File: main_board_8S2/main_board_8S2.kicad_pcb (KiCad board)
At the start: 2 copper layers, 114.3 x 86.4 mm, 47 parts

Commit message: Схемы и платы обновлены в связи с переименованием футпринта стойки VMH-STA-DA5
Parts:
- VMH1, VMH2, VMH3, VMH4: footprint KCL:STA-DA5 -> KCL:VMH-STA-DA5

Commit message: Платы скорректированы с учётом изменений в ФП переключателей
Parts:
- SA1, SA2: value SWITCH_SPECIAL_SK-42D01-G -> SWITCH_GENERAL_04P_02T
- SA3: value SWITCH_BLOCK_05 -> SWITCH_GENERAL_01P_01T_NO_05U
- SB1: value SWITCH_BUTTON_NO_01 -> SWITCH_BUTTON_NON-LOCK_01P_01T_NO
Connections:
- XP2 pad 1: Net-(SA2-Pad11) -> Net-(SA2-PadCOM2)
- XP2 pad 2: Net-(SA2-Pad2) -> Net-(SA2-PadCOM1)
- XS2 pad 1: Net-(SA2-Pad11) -> Net-(SA2-PadCOM2)
- XS2 pad 2: Net-(SA2-Pad2) -> Net-(SA2-PadCOM1)
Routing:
- net Net-(SA2-PadCOM1): track 0.00 -> 96.5 mm
- net Net-(SA2-Pad2): track 96.5 -> 0.00 mm
- net Net-(SA2-PadCOM2): track 0.00 -> 56.0 mm
- net Net-(SA2-Pad11): track 56.0 -> 0.00 mm

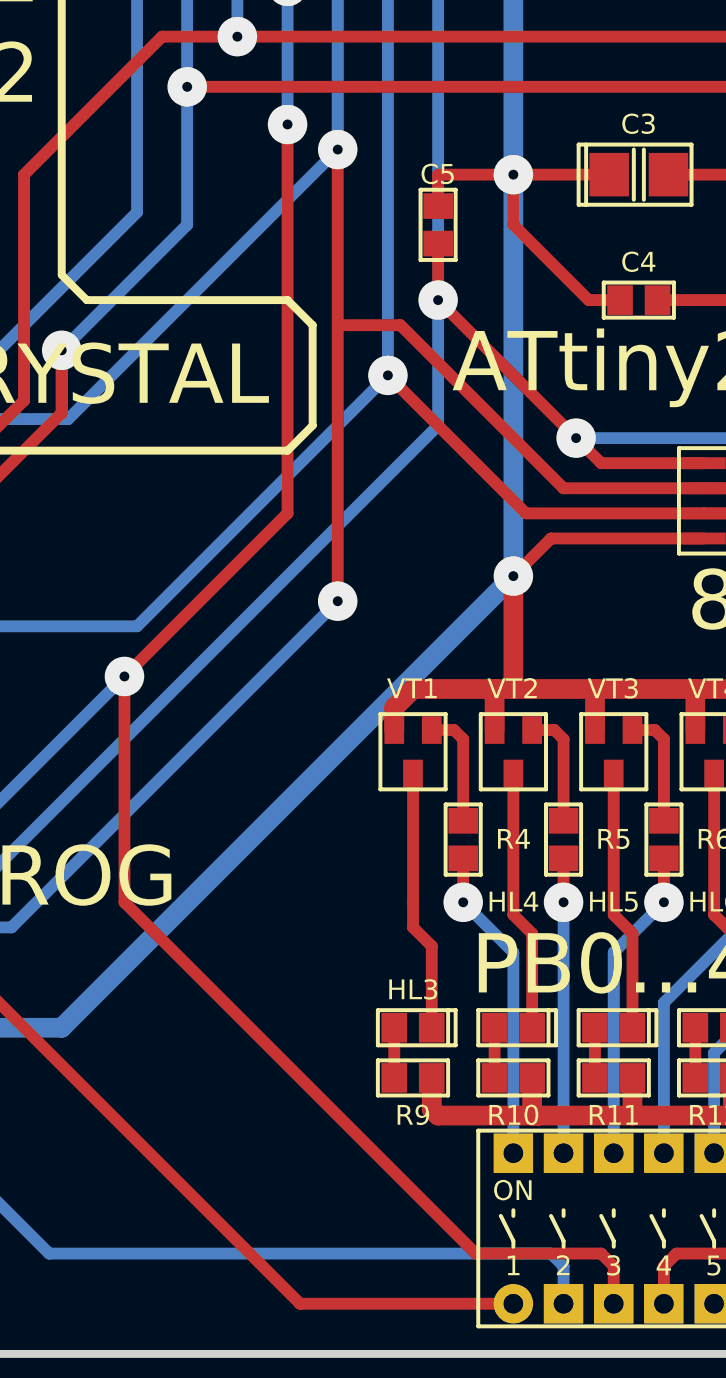
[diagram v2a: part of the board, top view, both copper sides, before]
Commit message: Незначительно оптимизирована трассировка
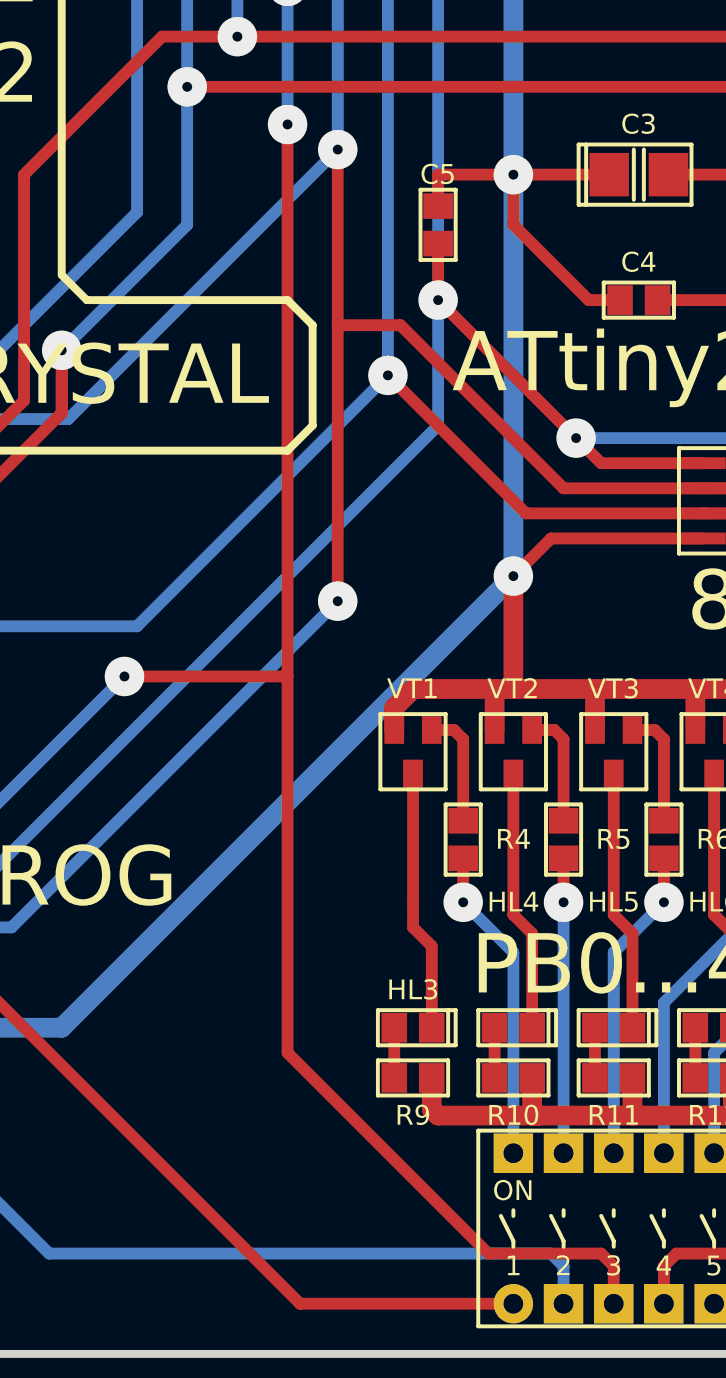
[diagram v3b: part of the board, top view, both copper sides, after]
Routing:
- net /PB2: track 189.1 -> 190.1 mm
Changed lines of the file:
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@@
     (thickness 1.5)
     (drawings 48)
-    (tracks 374)
+    (tracks 373)
     (zones 0)
     (modules 47)
@@
   (title_block
     (title main_board_8S2)
-    (date 2019-09-04)
+    (date 2019-09-07)
     (rev 1)
     (company "Igor Vladimirovich Ivanov")
@@
     (add_net "Net-(R8-Pad1)")
     (add_net "Net-(R8-Pad2)")
-    (add_net "Net-(SA1-PadNO1)")
-    (add_net "Net-(SA1-PadNO2)")
     (add_net "Net-(SA2-PadCOM1)")
     (add_net "Net-(SA2-PadCOM2)")
-    (add_net "Net-(SA2-PadNC1)")
-    (add_net "Net-(SA2-PadNC2)")
-    (add_net "Net-(SA2-PadNC3)")
-    (add_net "Net-(SA2-PadNC4)")
-    (add_net "Net-(VMH1-Pad0)")
-    (add_net "Net-(VMH2-Pad0)")
-    (add_net "Net-(VMH3-Pad0)")
-    (add_net "Net-(VMH4-Pad0)")
-    (add_net "Net-(XP2-Pad3)")
     (add_net V)
   )
@@
   (segment (start 100.33 116.84) (end 102.235 114.935) (width 0.6) (layer B.Cu) (net 9))
   (segment (start 151.64 104.775) (end 157.48 104.775) (width 0.6) (layer F.Cu) (net 9))
-  (segment (start 140.97 144.78) (end 140.97 142.875) (width 0.6) (layer F.Cu) (net 10))
-  (segment (start 140.97 142.875) (end 140.335 142.24) (width 0.6) (layer F.Cu) (net 10))
-  (segment (start 116.205 113.03) (end 124.46 104.775) (width 0.6) (layer F.Cu) (net 10))
   (segment (start 108.585 120.65) (end 116.205 113.03) (width 0.6) (layer B.Cu) (net 10))
   (via (at 116.205 113.03) (size 2) (drill 0.5) (layers F.Cu B.Cu) (net 10))
@@
   (segment (start 172.72 78.105) (end 172.72 74.93) (width 0.6) (layer B.Cu) (net 10))
   (via (at 172.72 78.105) (size 2) (drill 0.5) (layers F.Cu B.Cu) (net 10))
-  (segment (start 124.46 104.775) (end 124.46 85.09) (width 0.6) (layer F.Cu) (net 10))
-  (segment (start 116.205 124.46) (end 116.205 113.03) (width 0.6) (layer F.Cu) (net 10))
-  (segment (start 140.335 142.24) (end 133.985 142.24) (width 0.6) (layer F.Cu) (net 10))
-  (segment (start 133.985 142.24) (end 116.205 124.46) (width 0.6) (layer F.Cu) (net 10))
   (segment (start 124.46 78.105) (end 172.72 78.105) (width 0.6) (layer F.Cu) (net 10))
   (segment (start 172.72 86.36) (end 172.72 78.105) (width 0.6) (layer F.Cu) (net 10))
   (segment (start 155.575 103.505) (end 172.72 86.36) (width 0.6) (layer F.Cu) (net 10))
   (segment (start 151.64 103.505) (end 155.575 103.505) (width 0.6) (layer F.Cu) (net 10))
+  (segment (start 116.205 113.03) (end 124.46 113.03) (width 0.6) (layer F.Cu) (net 10))
+  (segment (start 124.46 132.08) (end 124.46 85.09) (width 0.6) (layer F.Cu) (net 10))
+  (segment (start 134.62 142.24) (end 124.46 132.08) (width 0.6) (layer F.Cu) (net 10))
+  (segment (start 140.335 142.24) (end 134.62 142.24) (width 0.6) (layer F.Cu) (net 10))
+  (segment (start 140.97 144.78) (end 140.97 142.875) (width 0.6) (layer F.Cu) (net 10))
+  (segment (start 140.97 142.875) (end 140.335 142.24) (width 0.6) (layer F.Cu) (net 10))
   (segment (start 102.235 92.71) (end 102.235 94.935) (width 0.6) (layer F.Cu) (net 11))
   (segment (start 101.6 92.075) (end 102.235 92.71) (width 0.6) (layer F.Cu) (net 11))
@@
   (segment (start 153.205 115.74) (end 153.67 116.205) (width 0.6) (layer F.Cu) (net 33))
   (segment (start 152.08 115.74) (end 153.205 115.74) (width 0.6) (layer F.Cu) (net 33))
-  (segment (start 198.12 74.93) (end 201.93 78.74) (width 1) (layer B.Cu) (net 35))
-  (segment (start 199.75 126) (end 202.25 126) (width 1) (layer B.Cu) (net 35))
-  (segment (start 201.93 95.29) (end 201.93 78.74) (width 1) (layer B.Cu) (net 35))
-  (segment (start 201.93 82.55) (end 197.945 82.55) (width 1) (layer B.Cu) (net 35))
-  (segment (start 190.5 74.93) (end 198.12 74.93) (width 1) (layer B.Cu) (net 35))
-  (segment (start 189.23 123.19) (end 189.23 76.2) (width 1) (layer B.Cu) (net 35))
-  (segment (start 199.75 126) (end 192.04 126) (width 1) (layer B.Cu) (net 35))
-  (segment (start 189.23 76.2) (end 190.5 74.93) (width 1) (layer B.Cu) (net 35))
-  (segment (start 192.04 126) (end 189.23 123.19) (width 1) (layer B.Cu) (net 35))
-  (segment (start 194.93 120) (end 199.75 120) (width 1) (layer B.Cu) (net 36))
-  (segment (start 191.945 117.015) (end 194.93 120) (width 1) (layer B.Cu) (net 36))
-  (segment (start 202.25 120) (end 199.75 120) (width 1) (layer B.Cu) (net 36))
-  (segment (start 201.93 100.29) (end 191.945 100.29) (width 1) (layer B.Cu) (net 36))
-  (segment (start 191.945 117.015) (end 191.945 82.55) (width 1) (layer B.Cu) (net 36))
   (segment (start 102.87 120.65) (end 102.87 123.19) (width 1) (layer B.Cu) (net 34))
   (segment (start 102.87 123.19) (end 102.87 125.73) (width 1) (layer B.Cu) (net 34))
@@
   (segment (start 132.08 72.39) (end 135.89 72.39) (width 1) (layer B.Cu) (net 34))
   (segment (start 145.54 106.045) (end 137.795 106.045) (width 0.6) (layer F.Cu) (net 34))
+  (segment (start 198.12 74.93) (end 201.93 78.74) (width 1) (layer B.Cu) (net 35))
+  (segment (start 199.75 126) (end 202.25 126) (width 1) (layer B.Cu) (net 35))
+  (segment (start 201.93 95.29) (end 201.93 78.74) (width 1) (layer B.Cu) (net 35))
+  (segment (start 201.93 82.55) (end 197.945 82.55) (width 1) (layer B.Cu) (net 35))
+  (segment (start 190.5 74.93) (end 198.12 74.93) (width 1) (layer B.Cu) (net 35))
+  (segment (start 189.23 123.19) (end 189.23 76.2) (width 1) (layer B.Cu) (net 35))
+  (segment (start 199.75 126) (end 192.04 126) (width 1) (layer B.Cu) (net 35))
+  (segment (start 189.23 76.2) (end 190.5 74.93) (width 1) (layer B.Cu) (net 35))
+  (segment (start 192.04 126) (end 189.23 123.19) (width 1) (layer B.Cu) (net 35))
+  (segment (start 194.93 120) (end 199.75 120) (width 1) (layer B.Cu) (net 36))
+  (segment (start 191.945 117.015) (end 194.93 120) (width 1) (layer B.Cu) (net 36))
+  (segment (start 202.25 120) (end 199.75 120) (width 1) (layer B.Cu) (net 36))
+  (segment (start 201.93 100.29) (end 191.945 100.29) (width 1) (layer B.Cu) (net 36))
+  (segment (start 191.945 117.015) (end 191.945 82.55) (width 1) (layer B.Cu) (net 36))
 )
